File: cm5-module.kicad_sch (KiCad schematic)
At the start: 0 parts

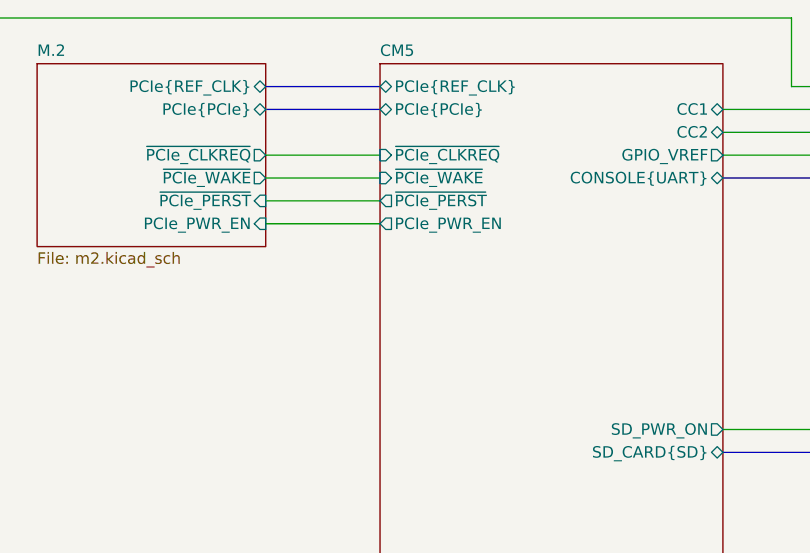
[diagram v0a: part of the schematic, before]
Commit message: [#1] Update CM5 connectors symbols, connect its misc pins
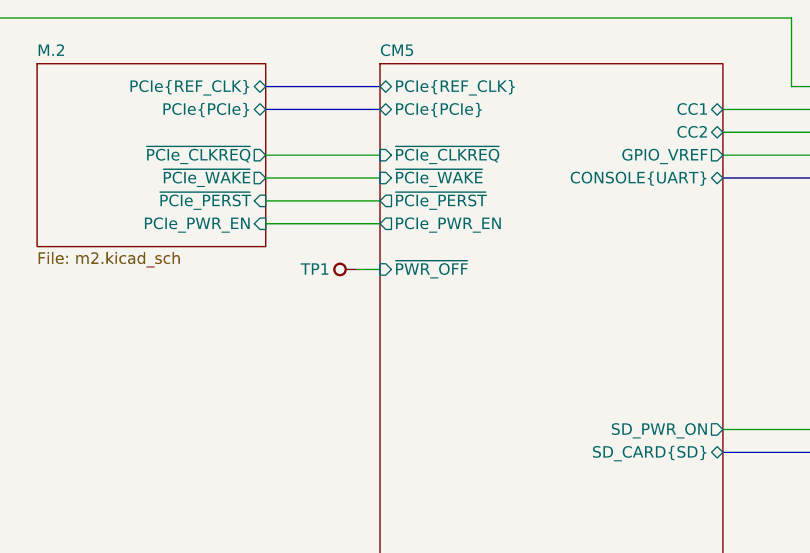
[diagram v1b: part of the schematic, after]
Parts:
- added TP1: TP_SMD_0.75mm, DW-footprints:TP_SMD_0.75mm, symbol DW-test-points:TP_SMD_0.75mm
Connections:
- new net CM5/~{PWR_OFF}: TP1.1
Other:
- sheet CM5 ports: added ~{PWR_OFF}; removed none
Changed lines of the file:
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@@
+		)
+	)
+	(wire
+		(pts
+			(xy 175.26 73.66) (xy 177.8 73.66)
+		)
+		(stroke
+			(width 0)
+			(type default)
 		)
 	)
@@
 			(width 0)
 			(type default)
+		)
+	)
+	(symbol
+		(lib_id "DW-test-points:TP_SMD_0.75mm")
+		(at 175.26 73.66 0)
+		(mirror y)
+		(unit 1)
+		(exclude_from_sim no)
+		(in_bom no)
+		(on_board yes)
+		(dnp no)
+		(property "Reference" "TP1"
+			(at 172.212 73.66 0)
+			(effects
+				(font
+					(size 1.27 1.27)
+					(thickness 0.15)
+				)
+				(justify left)
+			)
+		)
+		(property "Value" "TP_SMD_0.75mm"
+			(at 171.45 76.2 0)
+			(effects
+				(font
+					(size 1.27 1.27)
+					(thickness 0.15)
+				)
+				(justify left bottom)
+				(hide yes)
+			)
+		)
+		(property "Footprint" "DW-footprints:TP_SMD_0.75mm"
+			(at 171.45 78.74 0)
+			(effects
+				(font
+					(size 1.27 1.27)
+					(thickness 0.15)
+				)
+				(justify left bottom)
+				(hide yes)
+			)
+		)
+		(property "Datasheet" ""
+			(at 171.45 81.28 0)
+			(effects
+				(font
+					(size 1.27 1.27)
+					(thickness 0.15)
+				)
+				(justify left bottom)
+				(hide yes)
+			)
+		)
+		(property "Description" "Test point, SMD, round, 0.75mm diameter"
+			(at 171.45 83.82 0)
+			(effects
+				(font
+					(size 1.27 1.27)
+					(thickness 0.15)
+				)
+				(justify left bottom)
+				(hide yes)
+			)
+		)
+		(pin "1"
+		)
+		(instances
+			(project ""
+				(path "/090a8e41-87a8-4fb1-998b-60a2c0dc4cee"
+					(reference "TP1")
+					(unit 1)
+				)
+			)
 		)
 	)
@@
 			)
 		)
+		(pin "~{PWR_OFF}" input
+			(at 177.8 73.66 180)
+			(effects
+				(font
+					(size 1.27 1.27)
+				)
+				(justify left)
+			)
+		)

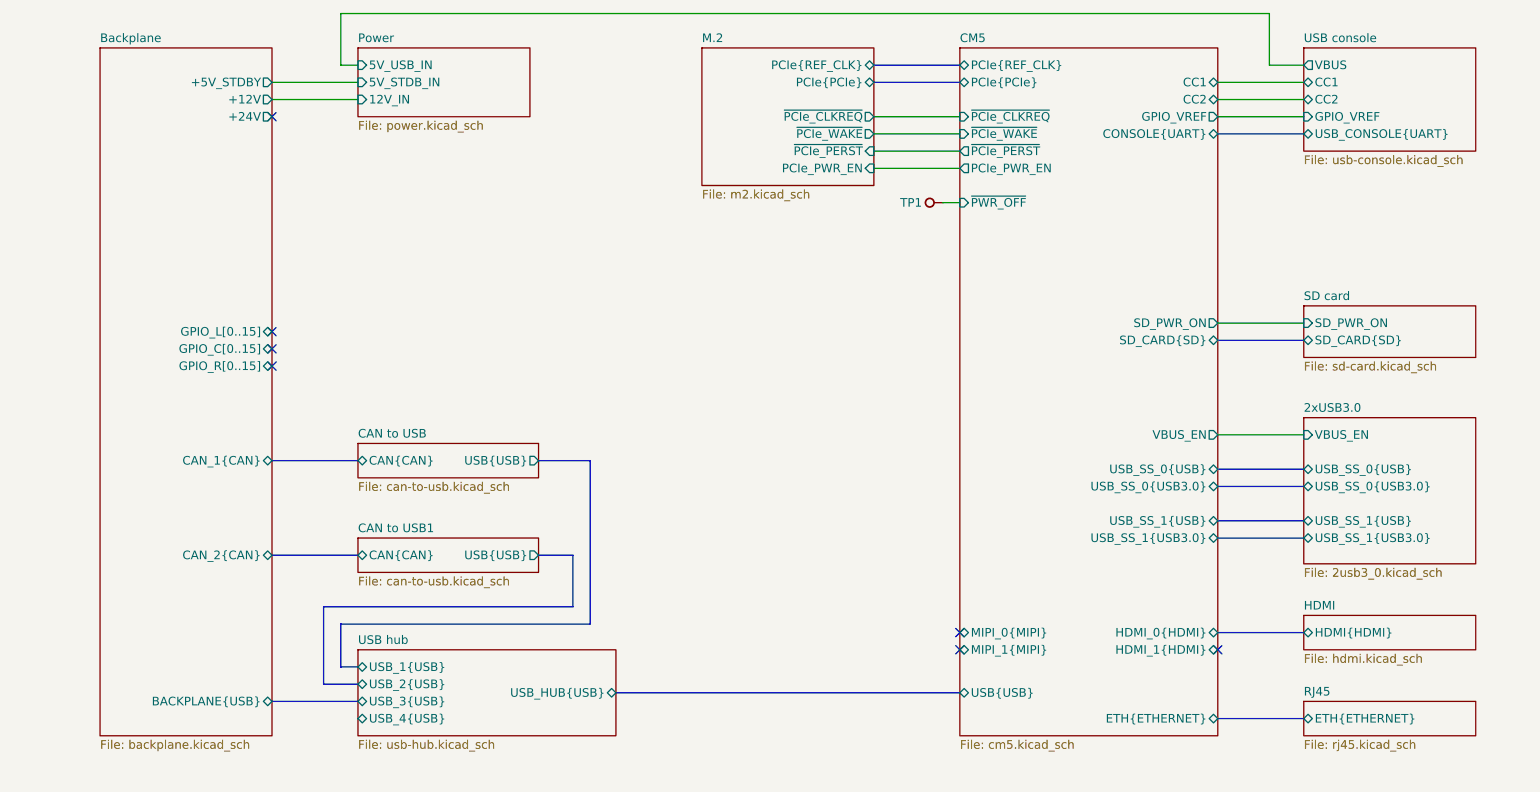
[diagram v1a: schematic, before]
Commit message: [#1] Add USB to CAN schematic, add power flags to 5V and 3V3
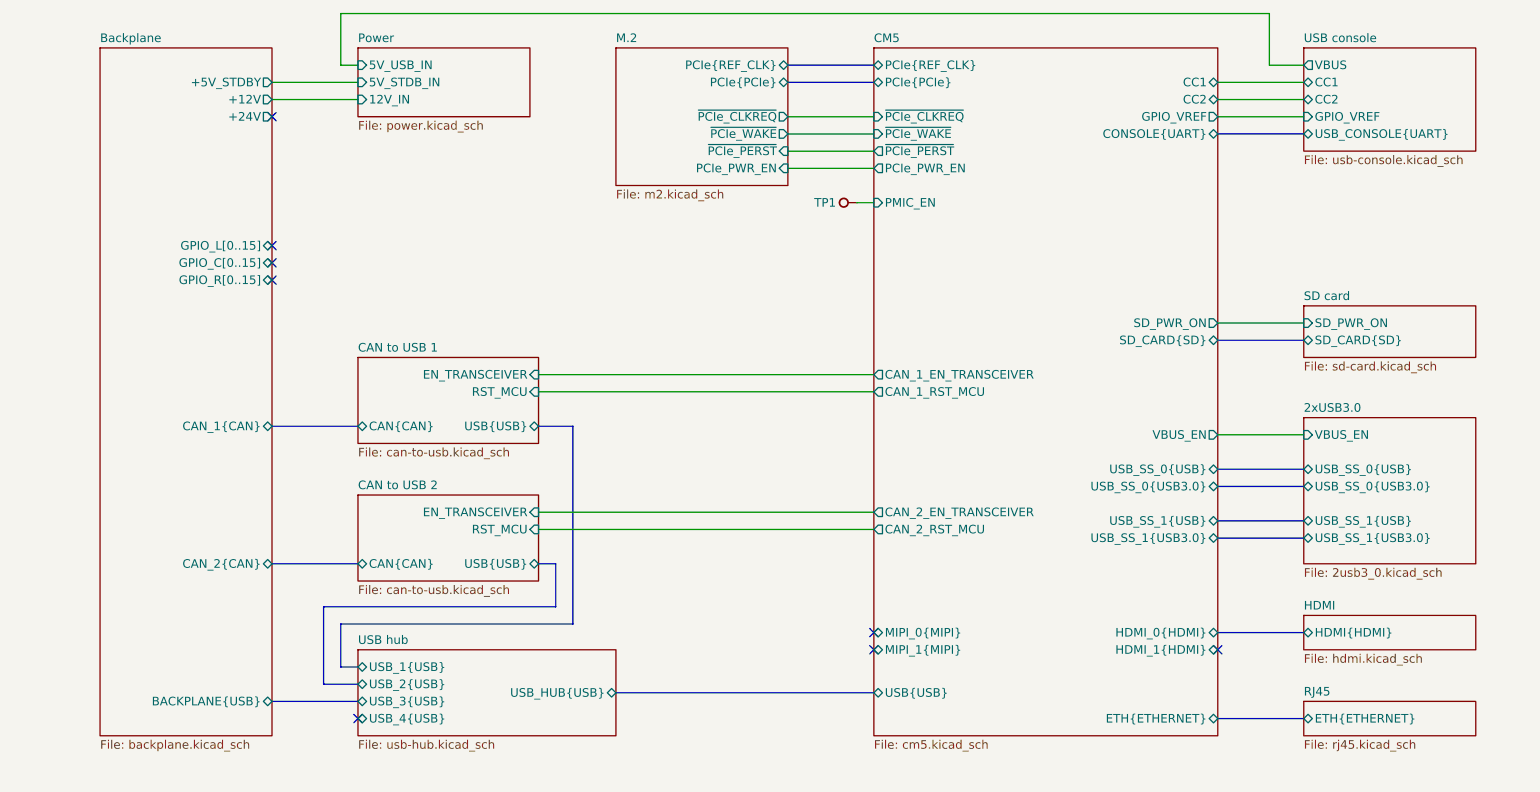
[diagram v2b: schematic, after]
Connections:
- net CM5/~{PWR_OFF} renamed CM5/PMIC_EN
- no-connect marks 7 -> 8
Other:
- sheet CAN to USB renamed CAN to USB 1
- sheet CAN to USB1 renamed CAN to USB 2
- sheet CAN to USB 1 ports: added EN_TRANSCEIVER, RST_MCU; removed none
- sheet CAN to USB 2 ports: added EN_TRANSCEIVER, RST_MCU; removed none
- sheet CM5 ports: added CAN_1_EN_TRANSCEIVER, CAN_1_RST_MCU, CAN_2_EN_TRANSCEIVER, CAN_2_RST_MCU, PMIC_EN; removed ~{PWR_OFF}
- moved on the sheet: TP1

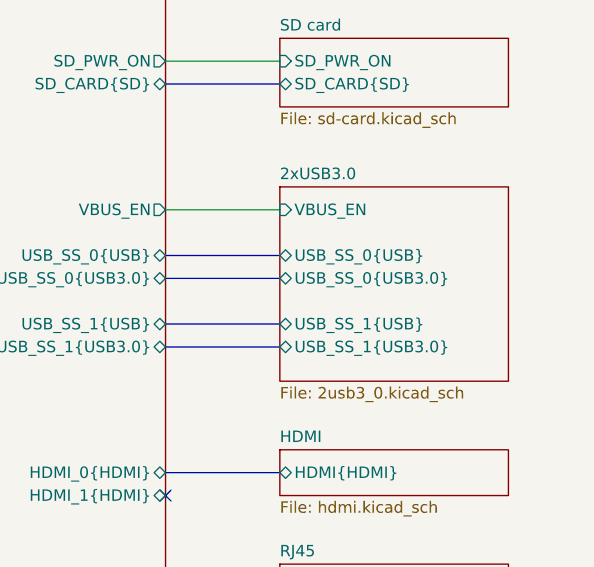
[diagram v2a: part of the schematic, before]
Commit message: [#1] Rename USB schematic sheet
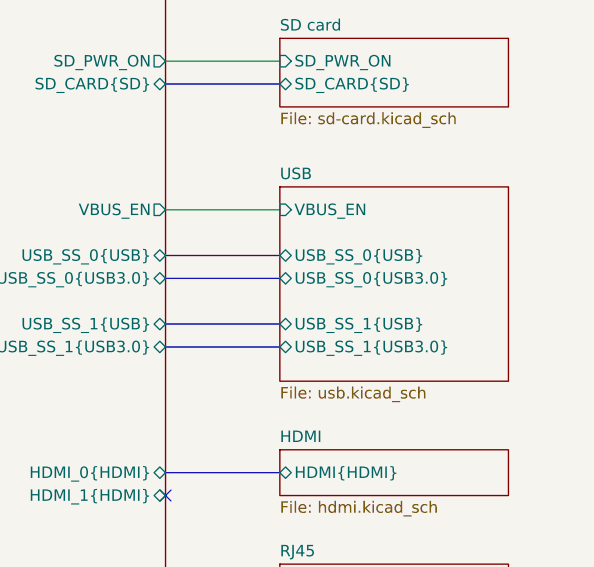
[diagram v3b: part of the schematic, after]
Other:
- sheet 2xUSB3.0 renamed USB
- sheet USB: file 2usb3_0.kicad_sch -> usb.kicad_sch
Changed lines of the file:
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@@
 			(color 255 255 194 1.0000)
 		)
-		(property "Sheetname" "2xUSB3.0"
+		(property "Sheetname" "USB"
 			(at 228.6 104.6984 0)
 			(effects
@@
 			)
 		)
-		(property "Sheetfile" "2usb3_0.kicad_sch"
+		(property "Sheetfile" "usb.kicad_sch"
 			(at 228.6 127.5846 0)
 			(effects

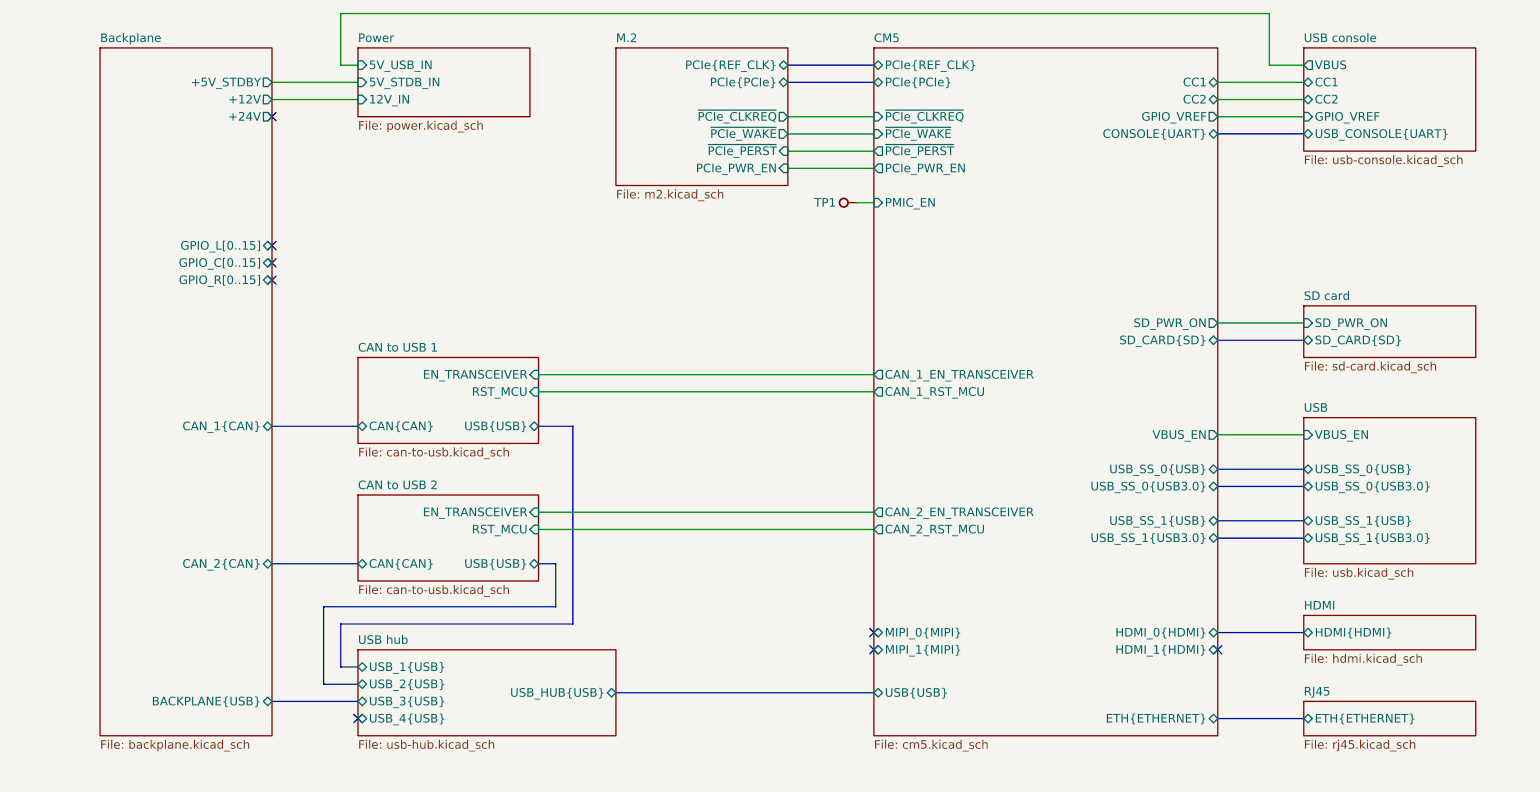
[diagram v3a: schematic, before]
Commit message: [#1] Add USB switch and 0R to USB hub data lines, minor schematic refactor
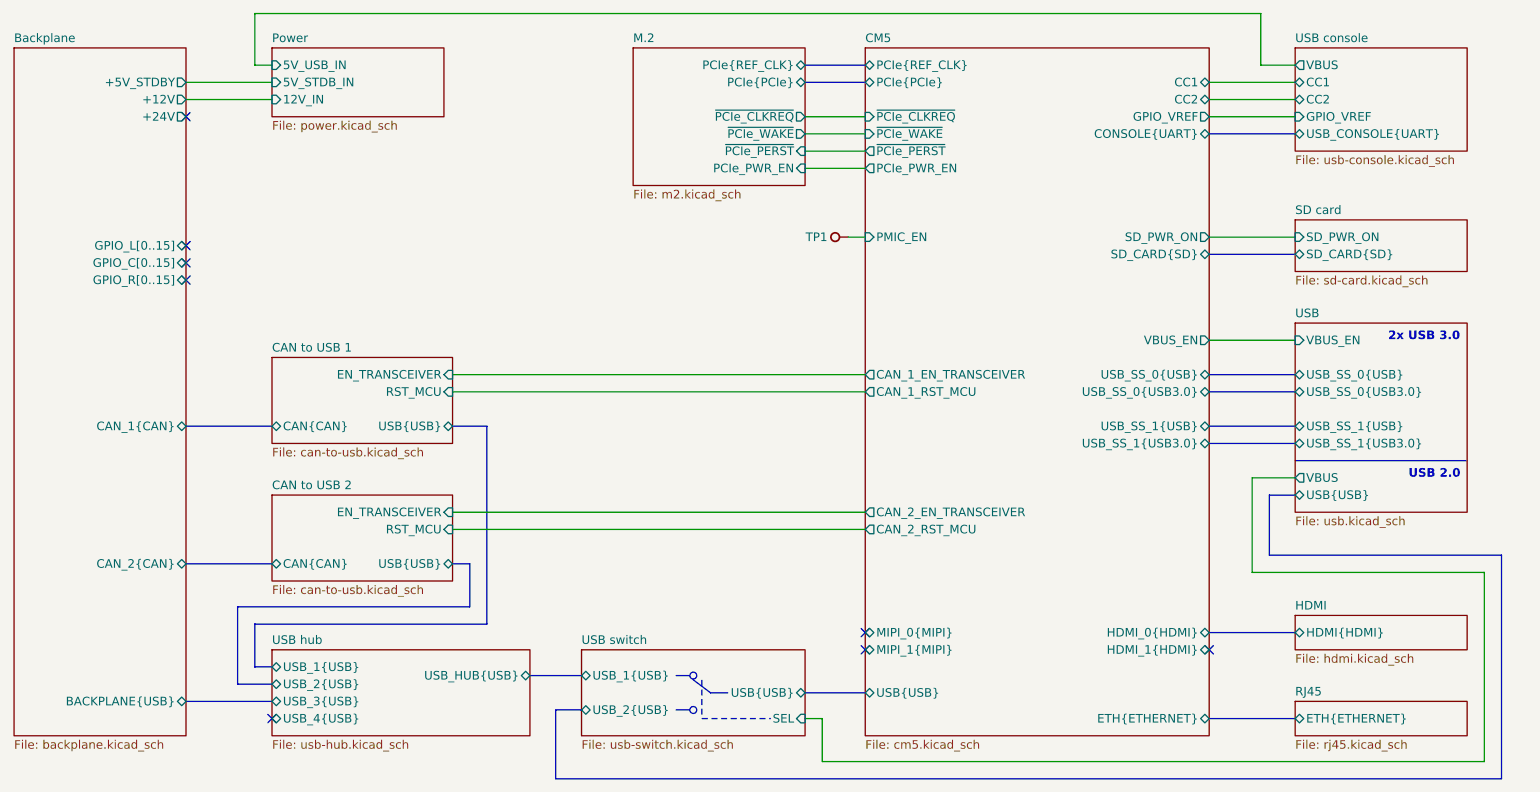
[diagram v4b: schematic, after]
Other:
- added sheet USB switch (usb-switch.kicad_sch)
- sheet USB ports: added USB{USB}, VBUS; removed none
- note added: "2x USB 3.0"
- note added: "USB 2.0"
- moved on the sheet: TP1

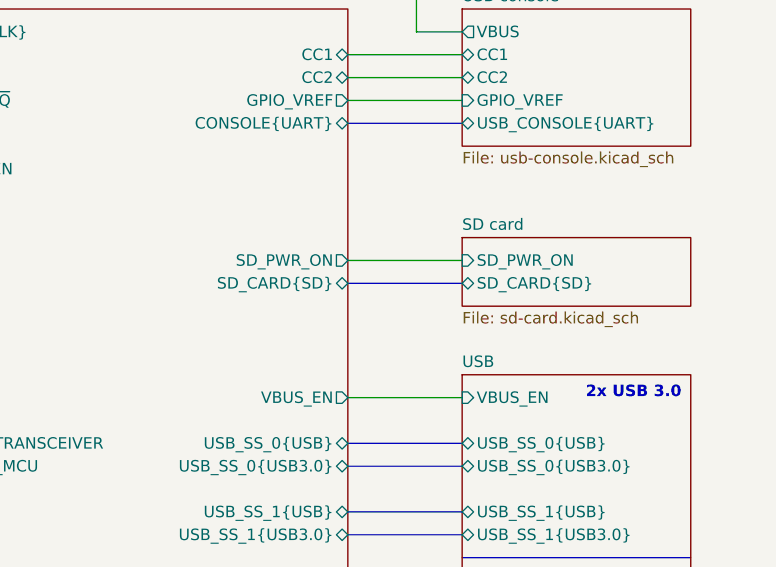
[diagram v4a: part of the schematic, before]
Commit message: [#3] WIP: Clear ERC, re-annotate schematic
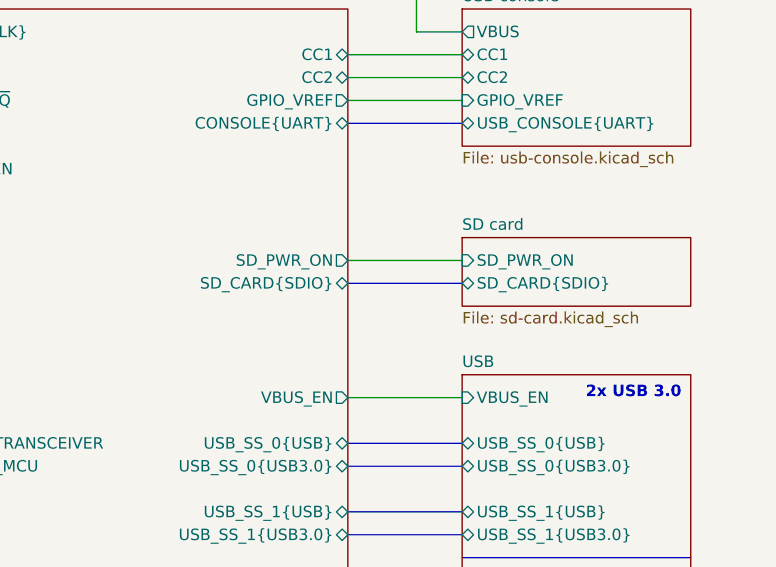
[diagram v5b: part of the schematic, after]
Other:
- sheet CM5 ports: added SD_CARD{SDIO}; removed SD_CARD{SD}
- sheet SD card ports: added SD_CARD{SDIO}; removed SD_CARD{SD}
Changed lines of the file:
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@@
-			)
-		)
-		(pin "SD_CARD{SD}" bidirectional
-			(at 227.33 81.28 180)
-			(effects
-				(font
-					(size 1.27 1.27)
-				)
-				(justify left)
 			)
 		)
 		(pin "SD_PWR_ON" input
 			(at 227.33 78.74 180)
+			(effects
+				(font
+					(size 1.27 1.27)
+				)
+				(justify left)
+			)
+		)
+		(pin "SD_CARD{SDIO}" bidirectional
+			(at 227.33 81.28 180)
 			(effects
 				(font
@@
 			)
 		)
-		(pin "SD_CARD{SD}" bidirectional
-			(at 214.63 81.28 0)
-			(effects
-				(font
-					(size 1.27 1.27)
-				)
-				(justify right)
-			)
-		)
 		(pin "USB_SS_0{USB}" bidirectional
 			(at 214.63 99.06 0)
@@
 			)
 		)
+		(pin "SD_CARD{SDIO}" bidirectional
+			(at 214.63 81.28 0)
+			(effects
+				(font
+					(size 1.27 1.27)
+				)
+				(justify right)
+			)
+		)

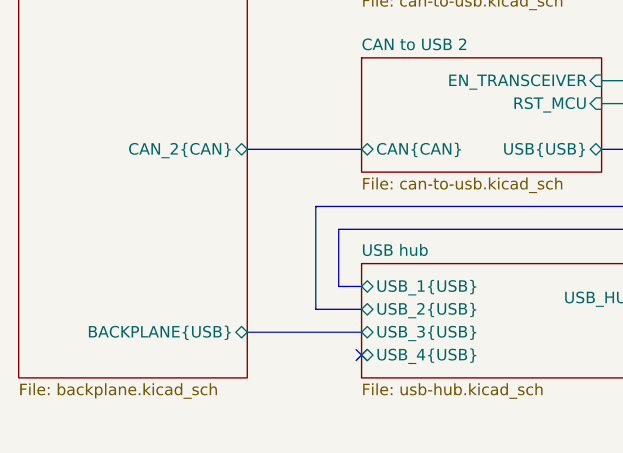
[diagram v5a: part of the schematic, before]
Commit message: [#3] Layout USB
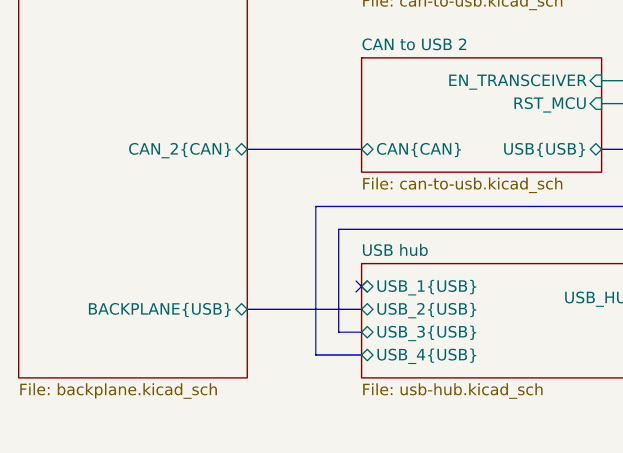
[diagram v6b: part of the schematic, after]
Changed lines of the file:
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@@
 	)
 	(no_connect
-		(at 76.2 149.86)
+		(at 76.2 142.24)
 	)
 	(no_connect
@@
 		)
 	)
-	(bus
-		(pts
-			(xy 63.5 147.32) (xy 76.2 147.32)
-		)
-		(stroke
-			(width 0)
-			(type default)
-		)
-	)
-	(bus
-		(pts
-			(xy 71.12 133.35) (xy 71.12 144.78)
-		)
-		(stroke
-			(width 0)
-			(type default)
-		)
-	)
 	(wire
 		(pts
@@
 		)
 	)
-	(bus
-		(pts
-			(xy 73.66 142.24) (xy 73.66 135.89)
-		)
-		(stroke
-			(width 0)
-			(type default)
-		)
-	)
 	(wire
 		(pts
@@
 		)
 	)
+	(bus
+		(pts
+			(xy 71.12 133.35) (xy 71.12 149.86)
+		)
+		(stroke
+			(width 0)
+			(type default)
+		)
+	)
 	(wire
 		(pts
@@
 	(bus
 		(pts
-			(xy 71.12 144.78) (xy 76.2 144.78)
-		)
-		(stroke
-			(width 0)
-			(type default)
-		)
-	)
-	(bus
-		(pts
 			(xy 105.41 133.35) (xy 71.12 133.35)
 		)
@@
 		(pts
 			(xy 214.63 55.88) (xy 227.33 55.88)
+		)
+		(stroke
+			(width 0)
+			(type default)
+		)
+	)
+	(bus
+		(pts
+			(xy 73.66 135.89) (xy 73.66 147.32)
 		)
 		(stroke
@@
 		)
 	)
+	(bus
+		(pts
+			(xy 76.2 149.86) (xy 71.12 149.86)
+		)
+		(stroke
+			(width 0)
+			(type default)
+		)
+	)
 	(wire
 		(pts
@@
 	(bus
 		(pts
-			(xy 76.2 142.24) (xy 73.66 142.24)
-		)
-		(stroke
-			(width 0)
-			(type default)
-		)
-	)
-	(bus
-		(pts
 			(xy 214.63 101.6) (xy 227.33 101.6)
 		)
@@
 		)
 	)
+	(bus
+		(pts
+			(xy 63.5 144.78) (xy 76.2 144.78)
+		)
+		(stroke
+			(width 0)
+			(type default)
+		)
+	)
 	(wire
 		(pts
@@
 		(pts
 			(xy 154.94 149.86) (xy 157.48 149.86)
+		)
+		(stroke
+			(width 0)
+			(type default)
+		)
+	)
+	(bus
+		(pts
+			(xy 73.66 147.32) (xy 76.2 147.32)
 		)
 		(stroke
@@
 		)
 		(pin "BACKPLANE{USB}" bidirectional
-			(at 63.5 147.32 0)
-			(effects
-				(font
+			(at 63.5 144.78 0)
+			(effects
+				(font
